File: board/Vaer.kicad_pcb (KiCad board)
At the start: 2 copper layers, 90 x 65 mm, 41 parts, among them J1 Conn_01x03_Pin, J2 Conn_01x03_Pin, J3 Conn_01x04_Pin, J4 GSB1C211110DS1HR, U1 BME280, U2 ESP32-S3-WROOM-1, U3 NCP1117-3.3_SOT223, U4 BQ24073RGT

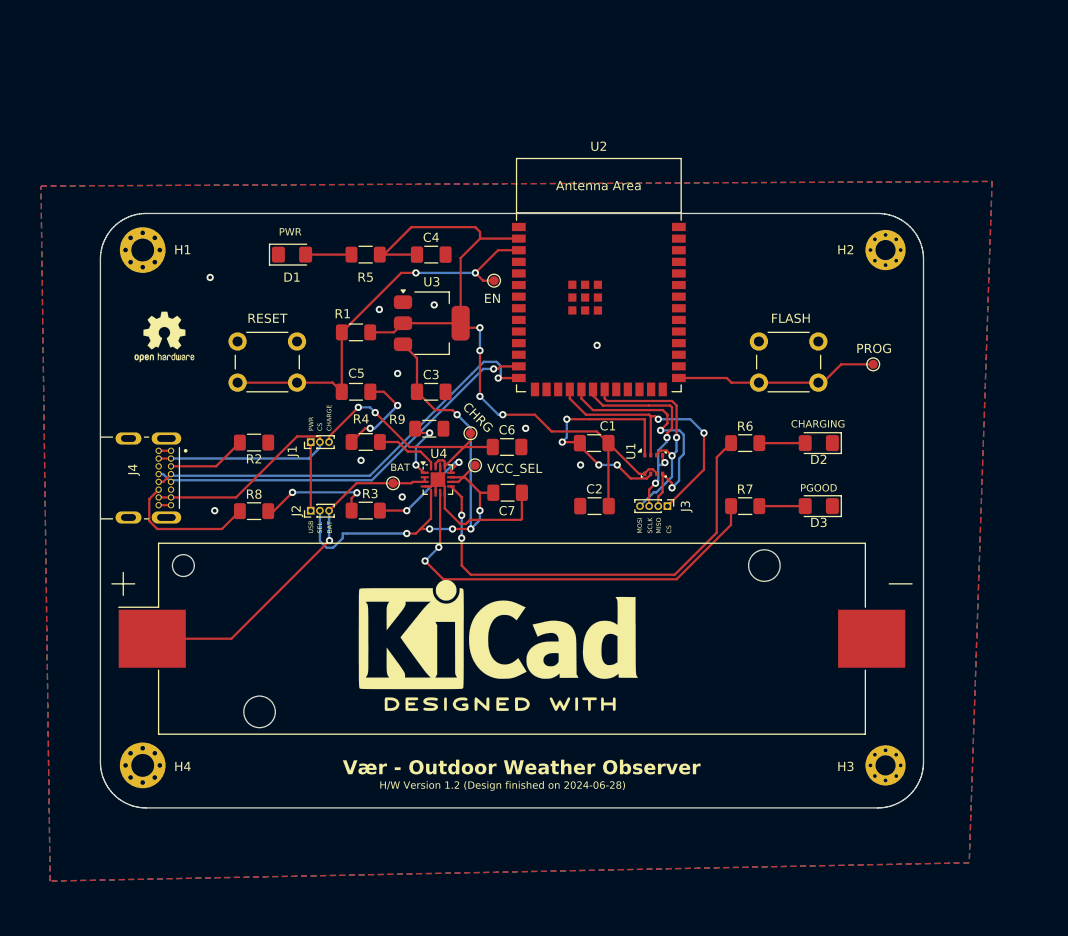
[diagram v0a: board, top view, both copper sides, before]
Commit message: :fire: Remove the GND pour on the back side of the PCB
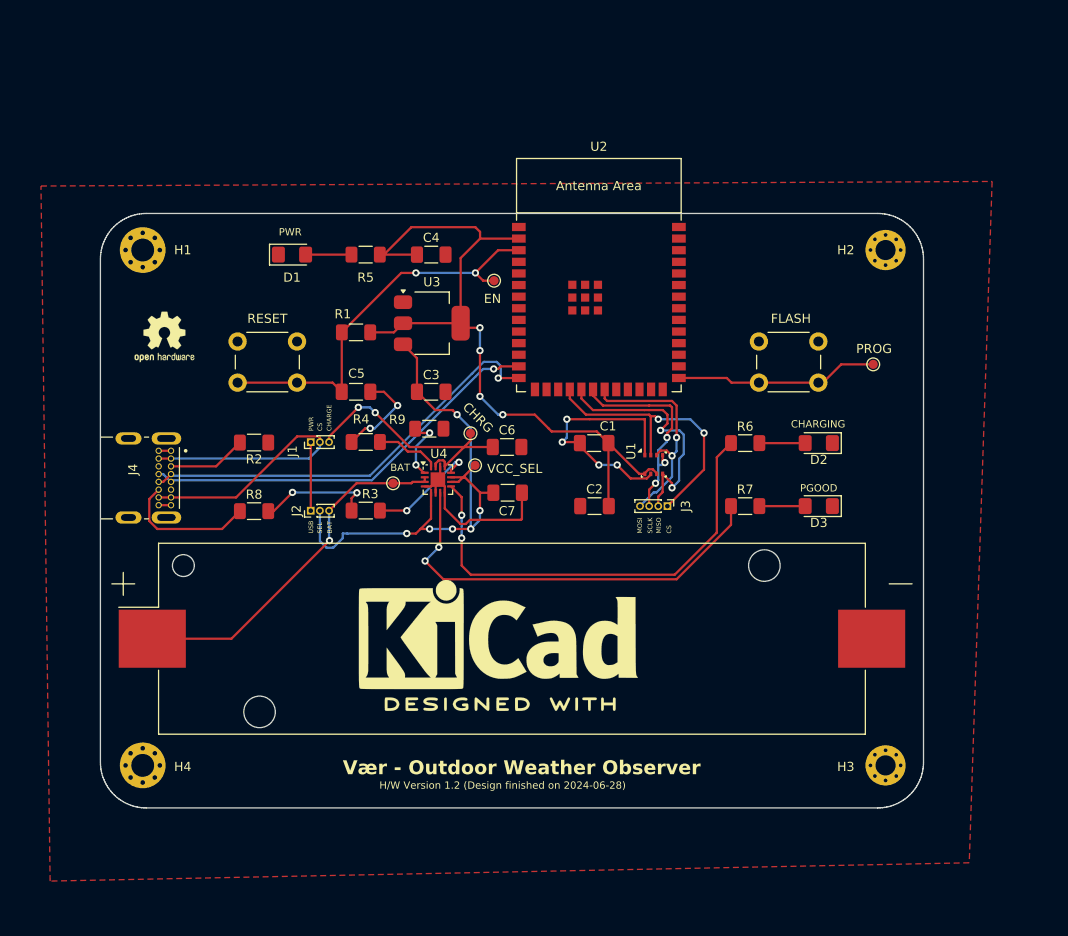
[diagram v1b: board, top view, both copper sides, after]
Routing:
- net GND: vias 18 -> 8
- removed copper zone on B.Cu, net GND
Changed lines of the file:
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@@
 	)
 	(via
-		(at 121.5 72.5)
-		(size 0.8)
-		(drill 0.4)
-		(layers "F.Cu" "B.Cu")
-		(free yes)
+		(at 139.5 90)
+		(size 0.8)
+		(drill 0.4)
+		(layers "F.Cu" "B.Cu")
 		(net 2)
 	)
 	(via
-		(at 139.5 90)
+		(at 141.5 90)
 		(size 0.8)
 		(drill 0.4)
@@
 	)
 	(via
-		(at 139.31 76.92)
-		(size 0.8)
-		(drill 0.4)
-		(layers "F.Cu" "B.Cu")
-		(free yes)
+		(at 106 93)
+		(size 0.8)
+		(drill 0.4)
+		(layers "F.Cu" "B.Cu")
 		(net 2)
 	)
 	(via
-		(at 131.5 86)
-		(size 0.8)
-		(drill 0.4)
-		(layers "F.Cu" "B.Cu")
-		(free yes)
+		(at 117.5 83.5)
+		(size 0.8)
+		(drill 0.4)
+		(layers "F.Cu" "B.Cu")
 		(net 2)
 	)
 	(via
-		(at 141.5 90)
+		(at 114.5 86)
 		(size 0.8)
 		(drill 0.4)
@@
 	)
 	(via
-		(at 106 93)
+		(at 135.5 87.5)
 		(size 0.8)
 		(drill 0.4)
@@
 	)
 	(via
-		(at 117.5 83.5)
-		(size 0.8)
-		(drill 0.4)
-		(layers "F.Cu" "B.Cu")
-		(net 2)
-	)
-	(via
-		(at 118 93.5)
-		(size 0.8)
-		(drill 0.4)
-		(layers "F.Cu" "B.Cu")
-		(free yes)
-		(net 2)
-	)
-	(via
-		(at 117.5 80)
-		(size 0.8)
-		(drill 0.4)
-		(layers "F.Cu" "B.Cu")
-		(free yes)
-		(net 2)
-	)
-	(via
-		(at 114.5 86)
-		(size 0.8)
-		(drill 0.4)
-		(layers "F.Cu" "B.Cu")
-		(net 2)
-	)
-	(via
-		(at 97.5 95)
-		(size 0.8)
-		(drill 0.4)
-		(layers "F.Cu" "B.Cu")
-		(free yes)
-		(net 2)
-	)
-	(via
-		(at 135.5 87.5)
-		(size 0.8)
-		(drill 0.4)
-		(layers "F.Cu" "B.Cu")
-		(net 2)
-	)
-	(via
-		(at 137.5 90)
-		(size 0.8)
-		(drill 0.4)
-		(layers "F.Cu" "B.Cu")
-		(free yes)
-		(net 2)
-	)
-	(via
-		(at 115.5 73)
-		(size 0.8)
-		(drill 0.4)
-		(layers "F.Cu" "B.Cu")
-		(free yes)
-		(net 2)
-	)
-	(via
 		(at 113.048008 93.048008)
 		(size 0.8)
 		(drill 0.4)
 		(layers "F.Cu" "B.Cu")
-		(net 2)
-	)
-	(via
-		(at 113.5 89.5)
-		(size 0.8)
-		(drill 0.4)
-		(layers "F.Cu" "B.Cu")
-		(free yes)
-		(net 2)
-	)
-	(via
-		(at 97 69.5)
-		(size 0.8)
-		(drill 0.4)
-		(layers "F.Cu" "B.Cu")
-		(free yes)
 		(net 2)
 	)
@@
 		(net 2)
 		(net_name "GND")
-		(layers "F&B.Cu")
+		(layer "F.Cu")
 		(hatch edge 0.5)
 		(connect_pads
@@
 		(min_thickness 0.25)
 		(filled_areas_thickness no)
-		(fill yes
+		(fill
 			(thermal_gap 0.5)
 			(thermal_bridge_width 0.5)

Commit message: :construction: Reorder the used components on the PCB
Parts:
- removed the REF** at (128.5, 108.5)
- added REF**: KiCad-Logo2_5mm_SilkScreen, Symbol:KiCad-Logo2_5mm_SilkScreen, F.Cu at (115.0, 107.0)
- added U5: USB6B1, Package_SO:SOIC-8_3.9x4.9mm_P1.27mm, F.Cu at (100.5, 85.0)
- H1, H4: footprint MountingHole:MountingHole_2.5mm_Pad_Via -> MountingHole:MountingHole_3.2mm_M3_Pad_Via
- H2, H3: footprint MountingHole:MountingHole_2.2mm_M2_Pad_Via -> MountingHole:MountingHole_3.2mm_M3_Pad_Via
- J1, J2: footprint Connector_PinHeader_1.00mm:PinHeader_1x03_P1.00mm_Vertical -> Connector_PinHeader_2.54mm:PinHeader_1x03_P2.54mm_Vertical
- J3: footprint Connector_PinHeader_1.00mm:PinHeader_1x04_P1.00mm_Vertical -> Connector_PinHeader_2.54mm:PinHeader_1x04_P2.54mm_Vertical
- moved TP1 68.1 mm to (107.7, 50.4)
- moved REF** 66.7 mm to (151.1, 107.0)
- moved TP3 43.2 mm to (117.3, 47.7)
- moved TP5 43.1 mm to (112.0, 49.1)
- moved TP4 40.7 mm to (125.1, 45.9)
- moved TP2 28.2 mm to (132.2, 41.9)
- moved J3 19.0 mm to (152.5, 76.3), turned to 180 degrees
- moved R3 17.1 mm to (131.1, 93.2)
- moved C2 16.4 mm to (154.1, 88.0), turned to 180 degrees
- moved C1 15.8 mm to (154.2, 92.1), turned to 180 degrees
- moved C7 10.6 mm to (140.0, 92.1)
- moved C6 10.5 mm to (140.0, 88.0)
- moved R4 9.97 mm to (122.2, 93.2)
- moved U4 9.53 mm to (131.0, 88.9)
- moved D2 6.64 mm to (169.7, 85.2)
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- renumbered PROG to TP1, EN to TP2, VCC_SEL to TP3, CHRG to TP4, BAT to TP5
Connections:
- J4 pad B6: D+ -> Net-(J4-DP2)
- J4 pad B7: D- -> Net-(J4-DN2)
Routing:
- net VCC_3V3: track 81.9 -> 0.00 mm, vias 4 -> 0
- net GND: track 73.2 -> 0.00 mm, vias 8 -> 0
- net VCC_SEL: track 63.2 -> 0.00 mm, vias 6 -> 0
- net ~{CHG}: track 49.8 -> 0.00 mm, vias 2 -> 0
- net ~{PGOOD}: track 46.9 -> 0.00 mm, vias 2 -> 0
- net D+: track 46.9 -> 0.00 mm, vias 1 -> 0
- net D-: track 45.0 -> 0.00 mm, vias 1 -> 0
- net EN: track 43.8 -> 0.00 mm, vias 2 -> 0
- net VCC_USB: track 40.3 -> 0.00 mm
- net VCC_BAT: track 39.4 -> 0.00 mm, vias 1 -> 0
- net CS: track 31.1 -> 0.00 mm, vias 2 -> 0
- net VCC_USB_CHARGE: track 28.4 -> 0.00 mm, vias 2 -> 0
- net MISO: track 27.9 -> 0.00 mm, vias 2 -> 0
- net MOSI: track 24.2 -> 0.00 mm, vias 2 -> 0
- net SCLK: track 23.4 -> 0.00 mm, vias 3 -> 0
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- removed copper zone on F.Cu, net GND
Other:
- board text added: "VCC"

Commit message: :bug: Fix the wiring of the USB dataline protection circuit
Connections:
- J4 pad A6: D+ -> D_{internal}+
- J4 pad A7: D- -> D_{internal}-
- J4 pad B6: Net-(J4-DP2) -> D_{internal}+
- J4 pad B7: Net-(J4-DN2) -> D_{internal}-
- U5 pad 2: Net-(J4-DN2) -> D_{internal}-
- U5 pad 3: Net-(J4-DP2) -> D_{internal}+
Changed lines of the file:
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@@
 	(net 55 "unconnected-(U2-SPIIO6{slash}GPIO35{slash}FSPID{slash}SUBSPID-Pad28)")
 	(net 56 "unconnected-(U2-MTDI{slash}GPIO41{slash}CLK_OUT1-Pad34)")
-	(net 57 "Net-(J4-DP2)")
-	(net 58 "Net-(J4-DN2)")
+	(net 57 "D_{internal}+")
+	(net 58 "D_{internal}-")
 	(net 59 "Net-(U5-GND-Pad4)")
 	(footprint "Connector_PinHeader_2.54mm:PinHeader_1x04_P2.54mm_Vertical"
@@
 		)
 		(fp_text user "${REFERENCE}"
-			(at 0 3.81 270)
+			(at 0 3.81 -90)
 			(layer "F.Fab")
 			(effects
@@
 		(tags "resistor handsolder")
 		(property "Reference" "R4"
-			(at -0.22 1.9 360)
+			(at -0.22 1.9 0)
 			(layer "F.SilkS")
 			(effects
@@
 		)
 		(property "Value" "1k13"
-			(at 0 1.82 360)
+			(at 0 1.82 0)
 			(layer "F.Fab")
 			(effects
@@
 		)
 		(fp_text user "${REFERENCE}"
-			(at 0 0 360)
+			(at 0 0 0)
 			(layer "F.Fab")
 			(effects
@@
 			(layers "F.Cu" "F.Paste" "F.Mask")
 			(roundrect_rratio 0.25)
-			(net 58 "Net-(J4-DN2)")
+			(net 58 "D_{internal}-")
 			(pinfunction "I/O1")
 			(pintype "passive")
@@
 			(layers "F.Cu" "F.Paste" "F.Mask")
 			(roundrect_rratio 0.25)
-			(net 57 "Net-(J4-DP2)")
+			(net 57 "D_{internal}+")
 			(pinfunction "I/O2")
 			(pintype "passive")
@@
 			(layers "*.Cu")
 			(remove_unused_layers no)
-			(net 16 "D+")
+			(net 57 "D_{internal}+")
 			(pinfunction "DP1")
 			(pintype "bidirectional")
@@
 			(layers "*.Cu")
 			(remove_unused_layers no)
-			(net 18 "D-")
+			(net 58 "D_{internal}-")
 			(pinfunction "DN1")
 			(pintype "bidirectional")
@@
 			(layers "*.Cu")
 			(remove_unused_layers no)
-			(net 57 "Net-(J4-DP2)")
+			(net 57 "D_{internal}+")
 			(pinfunction "DP2")
 			(pintype "bidirectional")
@@
 			(layers "*.Cu")
 			(remove_unused_layers no)
-			(net 58 "Net-(J4-DN2)")
+			(net 58 "D_{internal}-")
 			(pinfunction "DN2")
 			(pintype "bidirectional")

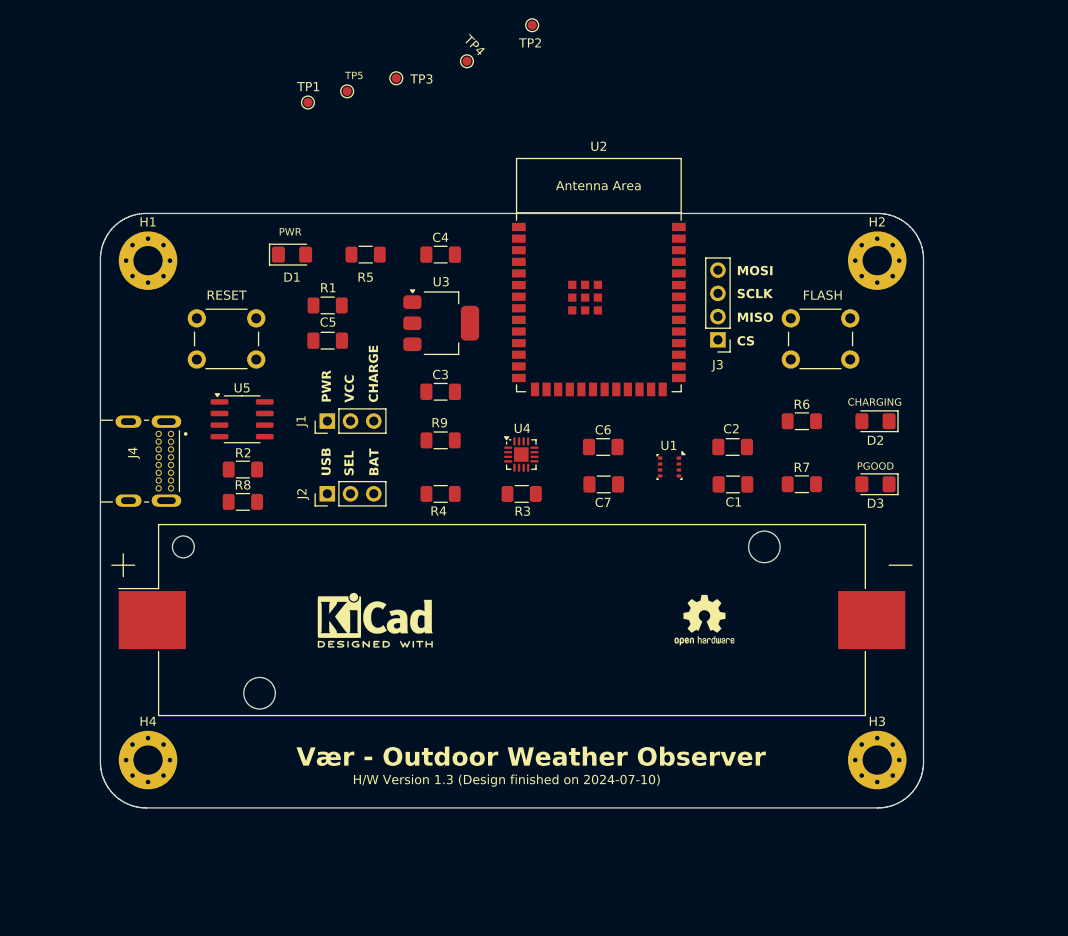
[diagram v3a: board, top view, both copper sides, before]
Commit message: :sparkles: Connect all components
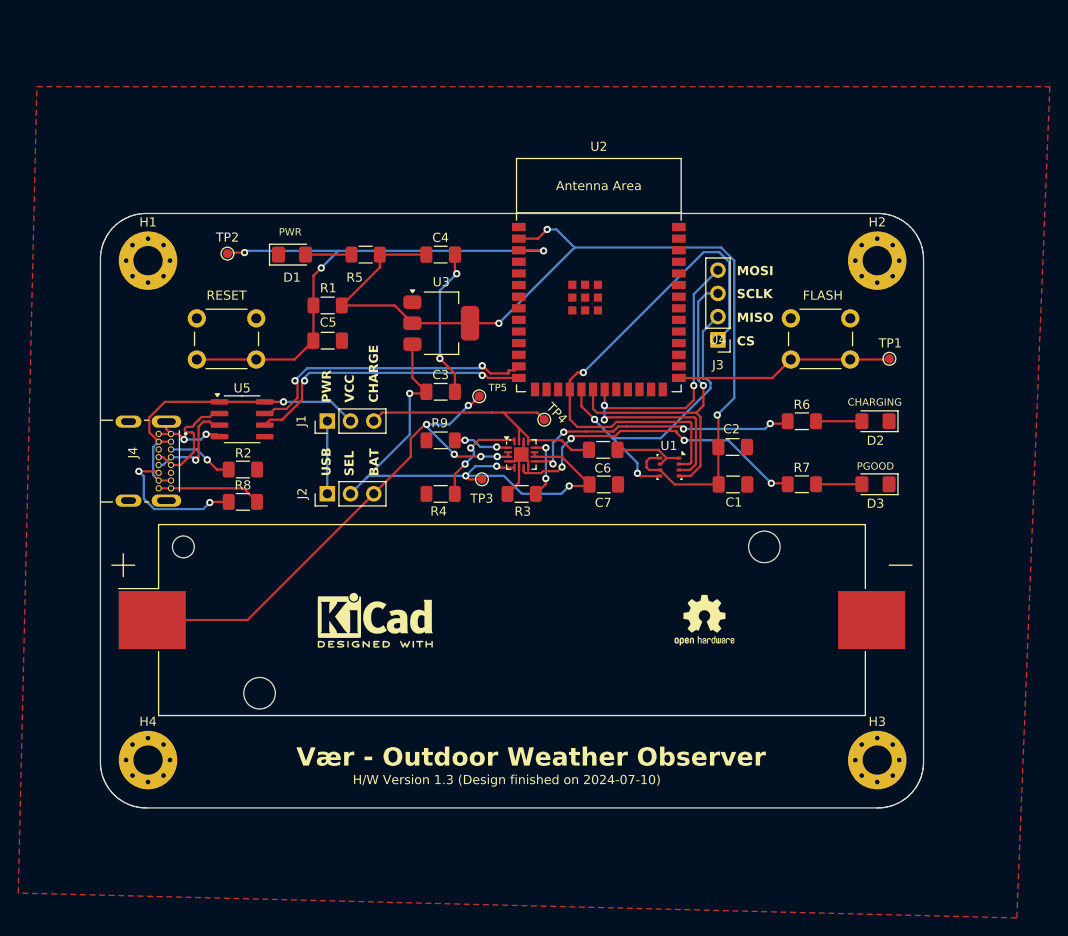
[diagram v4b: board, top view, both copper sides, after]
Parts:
- moved TP1 69.5 mm to (171.3, 78.4)
- moved TP3 44.8 mm to (126.7, 91.6)
- moved TP2 41.6 mm to (98.9, 66.9)
- moved TP4 40.1 mm to (133.5, 85.0)
- moved TP5 36.3 mm to (126.4, 82.5)
- moved C6 0.31 mm to (140.0, 88.3)
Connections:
- U5 pad 4: Net-(U5-GND-Pad4) -> GND
- U5 pad 5: Net-(U5-GND-Pad4) -> GND
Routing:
- net VCC_3V3: track 0.00 -> 103.7 mm, vias 0 -> 3
- net VCC_SEL: track 0.00 -> 62.5 mm, vias 0 -> 4
- net EN: track 0.00 -> 62.0 mm, vias 0 -> 3
- net VCC_BAT: track 0.00 -> 58.1 mm, vias 0 -> 5
- net CS: track 0.00 -> 56.6 mm, vias 0 -> 1
- net GND: track 0.00 -> 54.7 mm, vias 0 -> 4
- net MOSI: track 0.00 -> 46.2 mm, vias 0 -> 3
- net SCLK: track 0.00 -> 37.6 mm, vias 0 -> 1
- net MISO: track 0.00 -> 36.3 mm, vias 0 -> 2
- net ~{PGOOD}: track 0.00 -> 35.1 mm, vias 0 -> 4
- net VCC_USB: track 0.00 -> 34.1 mm, vias 0 -> 1
- net D-: track 0.00 -> 32.3 mm, vias 0 -> 2
- net VCC_USB_CHARGE: track 0.00 -> 32.2 mm
- net D+: track 0.00 -> 31.6 mm, vias 0 -> 2
- net ~{CHG}: track 0.00 -> 31.3 mm, vias 0 -> 4
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- added copper zone on F.Cu, net GND

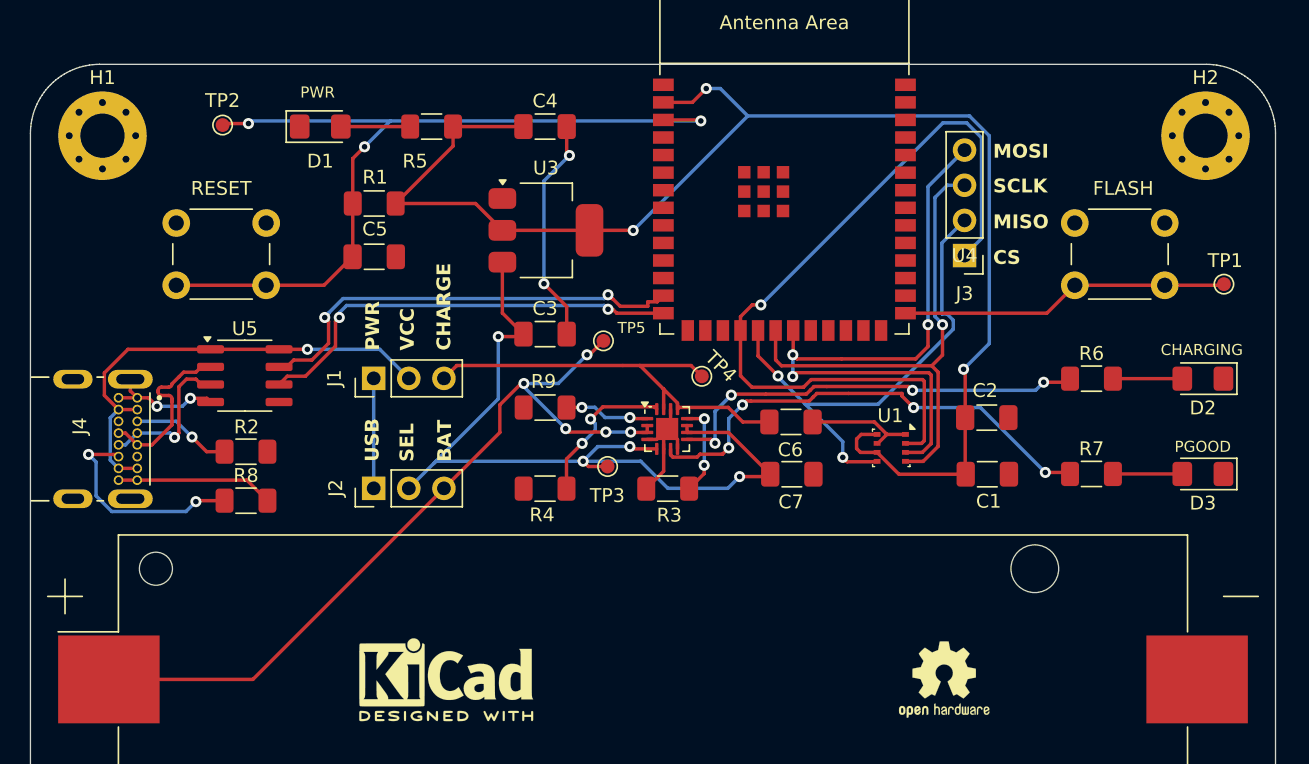
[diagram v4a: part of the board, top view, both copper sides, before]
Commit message: :recycle: Remove all connections and setup the min. for PCBWay
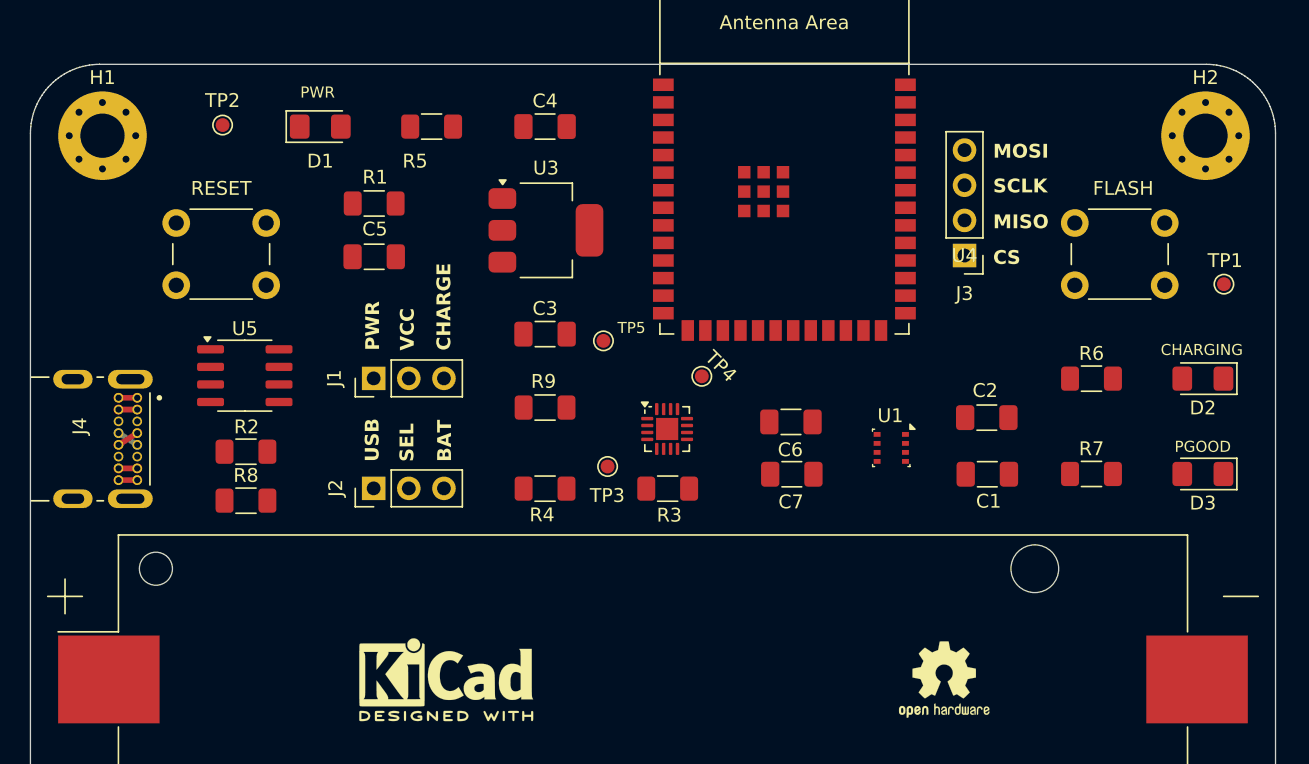
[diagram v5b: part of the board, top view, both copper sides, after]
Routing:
- net VCC_3V3: track 103.7 -> 0.00 mm, vias 3 -> 0
- net VCC_SEL: track 62.5 -> 0.00 mm, vias 4 -> 0
- net EN: track 62.0 -> 0.00 mm, vias 3 -> 0
- net VCC_BAT: track 58.1 -> 0.00 mm, vias 5 -> 0
- net CS: track 56.6 -> 0.00 mm, vias 1 -> 0
- net GND: track 54.7 -> 0.00 mm, vias 4 -> 0
- net MOSI: track 46.2 -> 0.00 mm, vias 3 -> 0
- net SCLK: track 37.6 -> 0.00 mm, vias 1 -> 0
- net MISO: track 36.3 -> 0.00 mm, vias 2 -> 0
- net ~{PGOOD}: track 35.1 -> 0.00 mm, vias 4 -> 0
- net VCC_USB: track 34.1 -> 0.00 mm, vias 1 -> 0
- net D-: track 32.3 -> 0.00 mm, vias 2 -> 0
- net VCC_USB_CHARGE: track 32.2 -> 0.00 mm
- net D+: track 31.6 -> 0.00 mm, vias 2 -> 0
- net ~{CHG}: track 31.3 -> 0.00 mm, vias 4 -> 0
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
